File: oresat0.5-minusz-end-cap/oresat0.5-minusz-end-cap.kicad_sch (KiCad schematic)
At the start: 28 parts

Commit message: Updated both oresat0.5 end caps. Fixed layout, and added patch antennas
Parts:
- removed C1, C10, C2, C3, C7: (no value), symbol minusz-end-cap-eagle-import:C-EU0402-B-NOSILK
- removed C12, C13, C15, C19, C4: (no value), symbol minusz-end-cap-eagle-import:C-EU0603-B-NOSILK
- removed CF2: (no value), symbol minusz-end-cap-eagle-import:J-HARWIN-M55-70X1242R
- removed D2: (no value), symbol minusz-end-cap-eagle-import:LED-GREEN0603
- removed R1, R2, R3, R4, R5, R6, R7: (no value), symbol minusz-end-cap-eagle-import:R-US_0402-B-NOSILK
- removed TP1, TP2, TP3, TP4, TP6, TP7: (no value), symbol minusz-end-cap-eagle-import:TEST-POINT
- removed U1: (no value), symbol minusz-end-cap-eagle-import:TCA9543A-PW
- removed U3, U4: (no value), symbol minusz-end-cap-eagle-import:HMC5883L-LGA-16
- added ANT1: GP.1575.25.2.A.02, oresat-misc:Taoglas-GPS-Patch-Antenna, symbol Device:Antenna
- added C1, C10, C12, C13, C2, C3, C4, C7: (no value), oresat0.5-minusz-end-cap:.0603-B-NOSILK, symbol oresat0-plusz-end-cap-eagle-import:C-EU0603-B-NOSILK
- added D2: (no value), oresat0.5-minusz-end-cap:LED-0603, symbol oresat0-plusz-end-cap-eagle-import:LED-GREEN0603
- added J1: (no value), oresat0.5-minusz-end-cap:HARWIN-M55-70X1242R, symbol oresat0-plusz-end-cap-eagle-import:J-HARWIN-M55-70X1242R
- added J2: U.FL-R-SMA, Connector_Coaxial:U.FL_Hirose_U.FL-R-SMT-1_Vertical, symbol Connector:Conn_Coaxial
- added R1, R10, R2, R3, R4, R5, R6, R7, R8, R9: (no value), oresat0.5-minusz-end-cap:.0603-B-NOSILK, symbol oresat0-plusz-end-cap-eagle-import:R-US_0603-B-NOSILK
- added R11, R12: NP, oresat0.5-minusz-end-cap:.0603-B-NOSILK, symbol oresat0-plusz-end-cap-eagle-import:R-US_0603-B-NOSILK
- added TP1, TP2, TP3, TP4, TP5, TP6, TP7, TP8: TEST-POINT-LARGE-SQUARE, oresat0.5-minusz-end-cap:1X01, symbol oresat0-plusz-end-cap-eagle-import:TEST-POINT-LARGE-SQUARE
- added U1: (no value), oresat0.5-minusz-end-cap:16-SSOP, symbol oresat0-plusz-end-cap-eagle-import:LTC4305
- added U2, U3: (no value), oresat0.5-minusz-end-cap:LGA-16(3X3), symbol oresat0-plusz-end-cap-eagle-import:MMC5883MA
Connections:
- net 3.3V: now also C1.1, C10.1, C2.1, C3.1, C4.1, C7.1, J1.5, J1.6, R10.2, R2.2, R3.2, R4.2, R5.2, R6.2, R7.2, R8.2, TP7.1, U1.7 (VCC), U2.13 (VDDIO), U2.2 (VDD), U3.13 (VDDIO), U3.2 (VDD)
- net GND: now also C1.2, C10.2, C12.2, C13.2, C2.2, C3.2, C4.2, C7.2, D2.C, J1.7, J1.8, J1.P$1 (SHIELDS), J1.P$2 (SHIELDS), J1.P$3 (SHIELDS), J1.P$4 (SHIELDS), J2.2 (Ext), R1.1, R9.1, TP8.1, U1.10 (ADR2), U1.4 (GND), U1.8 (ADR0), U1.9 (ADR1), U2.11 (GND), U2.9 (GND), U3.11 (GND), U3.9 (GND)
- net I2C-SCL: now also J1.3, J1.4, TP3.1, U1.5 (SCLIN)
- net I2C-SDA: now also J1.1, J1.2, TP6.1, U1.3 (SDAIN)
- new net: C12.1, U3.10 (CAP)
- new net: ANT1.1 (A), J2.1 (In)
- new net: R11.1, U3.15 (INT)
- new net: R12.1, U2.15 (INT)
- new net: R12.2, R8.1, U1.1 (~{ALERT2})
- new net: R9.2, U1.11 (READY)
- new net: R11.2, R3.1, U1.14 (~{ALERT1})
- new net: R1.2, U1.2 (~{ALERT})
- new net: R10.1, U1.6 (ENABLE)
- new net: D2.A, R2.1
- new net: C13.1, U2.10 (CAP)
- new net SCL1: R7.1, TP1.1, U1.12 (SCL1), U3.1 (SCL)
- new net SCL2: R4.1, TP4.1, U1.16 (SCL2), U2.1 (SCL)
- new net SDA1: R6.1, TP2.1, U1.13 (SDA1), U3.16 (SDA)
- new net SDA2: R5.1, TP5.1, U1.15 (SDA2), U2.16 (SDA)
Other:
- note added: "+X-Y Corner"
- note added: "-X+Y Corner"
- note added: "1.0"
- note added: "OreSat0.5 -Z End Cap"
- note removed: "+X+Y Corner"
- note removed: "-X-Y Corner"
- note removed: "2.0"
- note removed: "All caps are 0402 ceramic 10% X5R Vw>=16V unless marked"
- note removed: "All resistors 0402 +/- 1% unless marked"
- note removed: "OreSat +Z End Card"

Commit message: Updated both OreSat0.5 end caps and cleaned up errors
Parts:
- C1, C10, C12, C13, C2, C3, C4, C7: symbol oresat0-plusz-end-cap-eagle-import:C-EU0603-B-NOSILK -> oresat0.5-minusz-end-cap-eagle-import:C-EU0603-B-NOSILK
- D2: symbol oresat0-plusz-end-cap-eagle-import:LED-GREEN0603 -> oresat0.5-minusz-end-cap-eagle-import:LED-GREEN0603
- J1: symbol oresat0-plusz-end-cap-eagle-import:J-HARWIN-M55-70X1242R -> oresat0.5-minusz-end-cap-eagle-import:J-HARWIN-M55-70X1242R
- R1, R10, R11, R12, R2, R3, R4, R5, R6, R7, R8, R9: symbol oresat0-plusz-end-cap-eagle-import:R-US_0603-B-NOSILK -> oresat0.5-minusz-end-cap-eagle-import:R-US_0603-B-NOSILK
- TP1, TP2, TP3, TP4, TP5, TP6, TP7, TP8: symbol oresat0-plusz-end-cap-eagle-import:TEST-POINT-LARGE-SQUARE -> oresat0.5-minusz-end-cap-eagle-import:TEST-POINT-LARGE-SQUARE
- U1: symbol oresat0-plusz-end-cap-eagle-import:LTC4305 -> oresat0.5-minusz-end-cap-eagle-import:LTC4305
- U2, U3: value (none) -> MMC5883MA; symbol oresat0-plusz-end-cap-eagle-import:MMC5883MA -> oresat0.5-minusz-end-cap-eagle-import:MMC5883MA
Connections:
- no-connect marks 0 -> 4
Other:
- moved on the sheet: ANT1, C1, C10, C12, C13, C2, C3, C4, C7, D2, J1, J2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

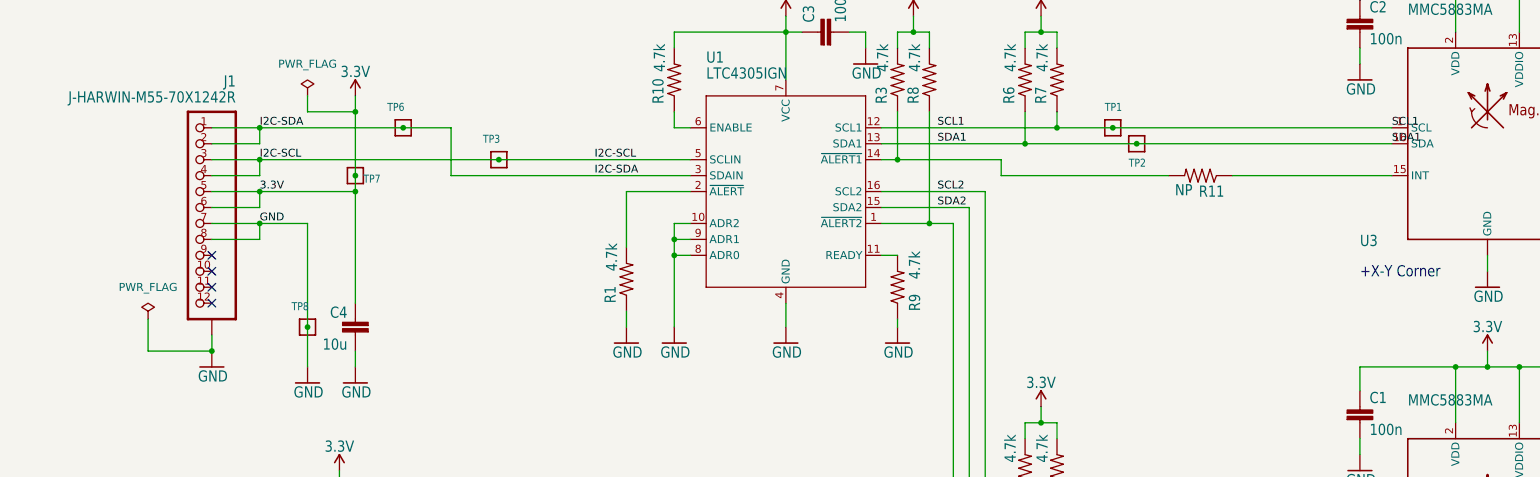
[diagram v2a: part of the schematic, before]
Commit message: OreSat0.5 end caps design review fixes
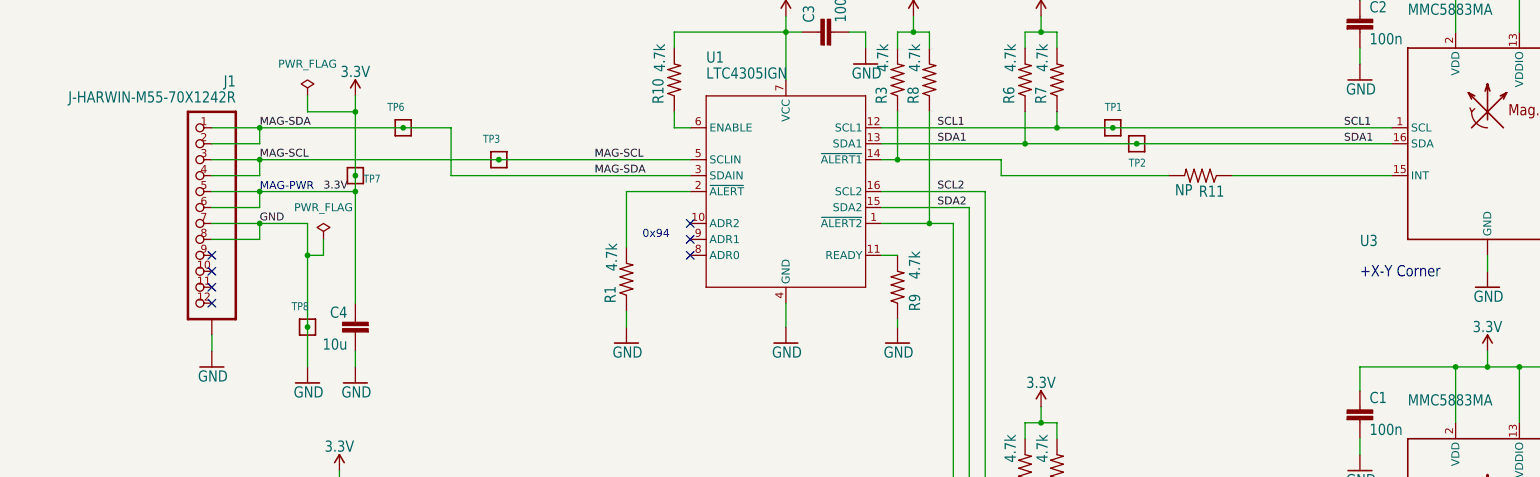
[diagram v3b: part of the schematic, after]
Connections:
- net GND: no longer U1.10 (ADR2), U1.8 (ADR0), U1.9 (ADR1)
- net I2C-SCL renamed MAG-SCL
- net I2C-SDA renamed MAG-SDA
- no-connect marks 4 -> 7
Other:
- note added: "0x94"
- note added: "MAG-PWR"
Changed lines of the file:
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@@
   (junction (at 124.46 119.38) (diameter 0) (color 0 0 0 0)
   )
-  (junction (at 175.26 132.08) (diameter 0) (color 0 0 0 0)
-  )
   (junction (at 193.04 96.52) (diameter 0) (color 0 0 0 0)
   )
@@
   (junction (at 233.68 158.75) (diameter 0) (color 0 0 0 0)
   )
-  (junction (at 175.26 129.54) (diameter 0) (color 0 0 0 0)
-  )
   (junction (at 304.8 88.9) (diameter 0) (color 0 0 0 0)
   )
+  (junction (at 116.84 132.08) (diameter 0) (color 0 0 0 0)
+  )
   (junction (at 233.68 96.52) (diameter 0) (color 0 0 0 0)
   )
@@
   )
   (junction (at 236.22 176.53) (diameter 0) (color 0 0 0 0)
-  )
-  (junction (at 101.6 147.32) (diameter 0) (color 0 0 0 0)
   )
   (no_connect (at 101.6 139.7))
@@
   (no_connect (at 101.6 137.16))
   (no_connect (at 101.6 134.62))
+  (no_connect (at 177.8 132.08))
+  (no_connect (at 177.8 129.54))
+  (no_connect (at 177.8 127))
   (wire (pts (xy 304.8 86.36) (xy 304.8 88.9))
     (stroke (width 0) (type default) (color 0 0 0 0))
@@
     (stroke (width 0) (type default) (color 0 0 0 0))
   )
-  (wire (pts (xy 91.44 147.32) (xy 91.44 142.24))
-    (stroke (width 0) (type default) (color 0 0 0 0))
-  )
   (wire (pts (xy 233.68 96.52) (xy 233.68 93.98))
     (stroke (width 0) (type default) (color 0 0 0 0))
@@
     (stroke (width 0) (type default) (color 0 0 0 0))
   )
-  (wire (pts (xy 175.26 129.54) (xy 177.8 129.54))
-    (stroke (width 0) (type default) (color 0 0 0 0))
-  )
   (wire (pts (xy 231.14 158.75) (xy 233.68 158.75))
     (stroke (width 0) (type default) (color 0 0 0 0))
@@
     (stroke (width 0) (type default) (color 0 0 0 0))
   )
+  (wire (pts (xy 116.84 132.08) (xy 119.38 132.08))
+    (stroke (width 0) (type default) (color 0 0 0 0))
+  )
   (wire (pts (xy 222.25 176.53) (xy 236.22 176.53))
     (stroke (width 0) (type default) (color 0 0 0 0))
@@
     (stroke (width 0) (type default) (color 0 0 0 0))
   )
-  (wire (pts (xy 175.26 143.51) (xy 175.26 132.08))
-    (stroke (width 0) (type default) (color 0 0 0 0))
-  )
   (wire (pts (xy 325.12 161.29) (xy 325.12 163.83))
     (stroke (width 0) (type default) (color 0 0 0 0))
@@
     (stroke (width 0) (type default) (color 0 0 0 0))
   )
-  (wire (pts (xy 175.26 132.08) (xy 175.26 129.54))
-    (stroke (width 0) (type default) (color 0 0 0 0))
-  )
   (wire (pts (xy 208.28 124.46) (xy 222.25 124.46))
     (stroke (width 0) (type default) (color 0 0 0 0))
@@
     (stroke (width 0) (type default) (color 0 0 0 0))
   )
-  (wire (pts (xy 175.26 127) (xy 177.8 127))
-    (stroke (width 0) (type default) (color 0 0 0 0))
-  )
   (wire (pts (xy 193.04 93.98) (xy 193.04 96.52))
     (stroke (width 0) (type default) (color 0 0 0 0))
@@
     (stroke (width 0) (type default) (color 0 0 0 0))
   )
-  (wire (pts (xy 175.26 132.08) (xy 177.8 132.08))
-    (stroke (width 0) (type default) (color 0 0 0 0))
-  )
   (wire (pts (xy 299.72 88.9) (xy 304.8 88.9))
     (stroke (width 0) (type default) (color 0 0 0 0))
   )
-  (wire (pts (xy 175.26 129.54) (xy 175.26 127))
-    (stroke (width 0) (type default) (color 0 0 0 0))
-  )
   (wire (pts (xy 236.22 171.45) (xy 236.22 176.53))
     (stroke (width 0) (type default) (color 0 0 0 0))
@@
     (stroke (width 0) (type default) (color 0 0 0 0))
   )
-  (wire (pts (xy 101.6 147.32) (xy 91.44 147.32))
+  (wire (pts (xy 116.84 132.08) (xy 116.84 143.51))
     (stroke (width 0) (type default) (color 0 0 0 0))
   )
@@
     (stroke (width 0) (type default) (color 0 0 0 0))
   )
-  (wire (pts (xy 116.84 127) (xy 116.84 143.51))
+  (wire (pts (xy 116.84 127) (xy 116.84 132.08))
     (stroke (width 0) (type default) (color 0 0 0 0))
   )
@@
   )
   (wire (pts (xy 248.92 114.3) (xy 231.14 114.3))
+    (stroke (width 0) (type default) (color 0 0 0 0))
+  )
+  (wire (pts (xy 119.38 129.54) (xy 119.38 132.08))
     (stroke (width 0) (type default) (color 0 0 0 0))
   )
@@
     (effects (font (size 2.032 2.032)) (justify left bottom))
   )
-  (label "I2C-SCL" (at 109.22 116.84 0)
+  (text "MAG-PWR" (at 109.22 121.92 0)
+    (effects (font (size 1.27 1.27)) (justify left bottom))
+  )
+  (text "0x94" (at 170.18 129.54 0)
+    (effects (font (size 1.27 1.27)) (justify left bottom))
+  )
+  (label "MAG-SCL" (at 109.22 116.84 0)
     (effects (font (size 1.2446 1.2446)) (justify left bottom))
   )
-  (label "I2C-SDA" (at 109.22 111.76 0)
+  (label "MAG-SDA" (at 109.22 111.76 0)
     (effects (font (size 1.2446 1.2446)) (justify left bottom))
   )
@@
     (effects (font (size 1.2446 1.2446)) (justify left bottom))
   )
-  (label "SCL1" (at 289.56 111.76 0)
+  (label "SCL1" (at 281.94 111.76 0)
     (effects (font (size 1.2446 1.2446)) (justify left bottom))
   )
-  (label "I2C-SDA" (at 162.56 119.38 0)
+  (label "MAG-SDA" (at 162.56 119.38 0)
     (effects (font (size 1.2446 1.2446)) (justify left bottom))
   )
-  (label "3.3V" (at 109.22 121.92 0)
+  (label "3.3V" (at 119.38 121.92 0)
     (effects (font (size 1.2446 1.2446)) (justify left bottom))
   )
@@
     (effects (font (size 1.2446 1.2446)) (justify left bottom))
   )
-  (label "I2C-SCL" (at 162.56 116.84 0)
+  (label "MAG-SCL" (at 162.56 116.84 0)
     (effects (font (size 1.2446 1.2446)) (justify left bottom))
   )
-  (label "SDA1" (at 289.56 114.3 0)
+  (label "SDA1" (at 281.94 114.3 0)
     (effects (font (size 1.2446 1.2446)) (justify left bottom))
   )
@@
     (pin "1")
   )
-  (symbol (lib_id "oresat0.5-minusz-end-cap-eagle-import:GND") (at 175.26 146.05 0) (mirror y) (unit 1)
-    (in_bom yes) (on_board yes)
-    (property "Reference" "#GND0103" (id 0) (at 175.26 146.05 0)
-      (effects (font (size 1.27 1.27)) hide)
-    )
-    (property "Value" "GND" (id 1) (at 177.8 148.59 0)
-      (effects (font (size 1.778 1.5113)) (justify left bottom))
-    )
-    (property "Footprint" "oresat0-plusz-end-cap:" (id 2) (at 175.26 146.05 0)
-      (effects (font (size 1.27 1.27)) hide)
-    )
-    (property "Datasheet" "" (id 3) (at 175.26 146.05 0)
-      (effects (font (size 1.27 1.27)) hide)
-    )
-    (pin "1")
-  )
   (symbol (lib_id "oresat0.5-minusz-end-cap-eagle-import:GND") (at 116.84 152.4 0) (mirror y) (unit 1)
     (in_bom yes) (on_board yes)
@@
     (pin "2")
   )
-  (symbol (lib_id "power:PWR_FLAG") (at 91.44 142.24 0) (unit 1)
+  (symbol (lib_id "power:PWR_FLAG") (at 119.38 129.54 0) (unit 1)
     (in_bom yes) (on_board yes) (fields_autoplaced)
-    (property "Reference" "#FLG0101" (id 0) (at 91.44 140.335 0)
-      (effects (font (size 1.27 1.27)) hide)
-    )
-    (property "Value" "PWR_FLAG" (id 1) (at 91.44 137.16 0))
-    (property "Footprint" "" (id 2) (at 91.44 142.24 0)
-      (effects (font (size 1.27 1.27)) hide)
-    )
-    (property "Datasheet" "~" (id 3) (at 91.44 142.24 0)
+    (property "Reference" "#FLG0101" (id 0) (at 119.38 127.635 0)
+      (effects (font (size 1.27 1.27)) hide)
+    )
+    (property "Value" "PWR_FLAG" (id 1) (at 119.38 124.46 0))
+    (property "Footprint" "" (id 2) (at 119.38 129.54 0)
+      (effects (font (size 1.27 1.27)) hide)
+    )
+    (property "Datasheet" "~" (id 3) (at 119.38 129.54 0)
       (effects (font (size 1.27 1.27)) hide)
     )
@@
       (reference "#GND0102") (unit 1) (value "GND") (footprint "oresat0-plusz-end-cap:")
     )
-    (path "/3d14e0e7-82bc-4dbb-9e62-5a07bc58df6c"
-      (reference "#GND0103") (unit 1) (value "GND") (footprint "oresat0-plusz-end-cap:")
-    )
     (path "/a60a1df8-eb53-419a-845c-a317b6139ba4"

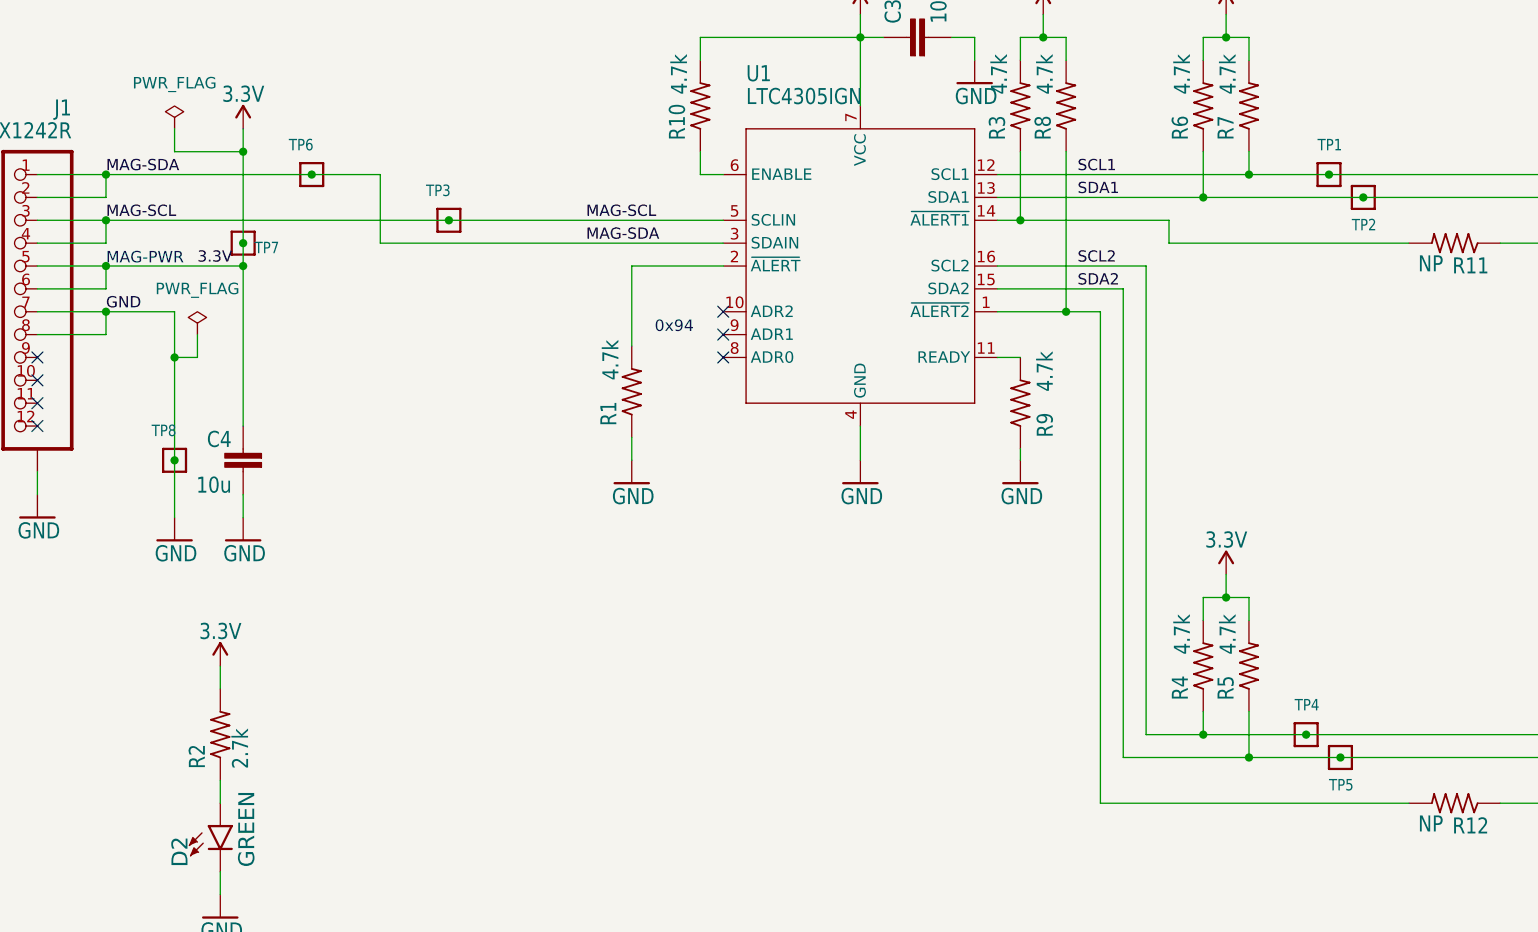
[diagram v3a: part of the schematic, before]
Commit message: Updated end caps
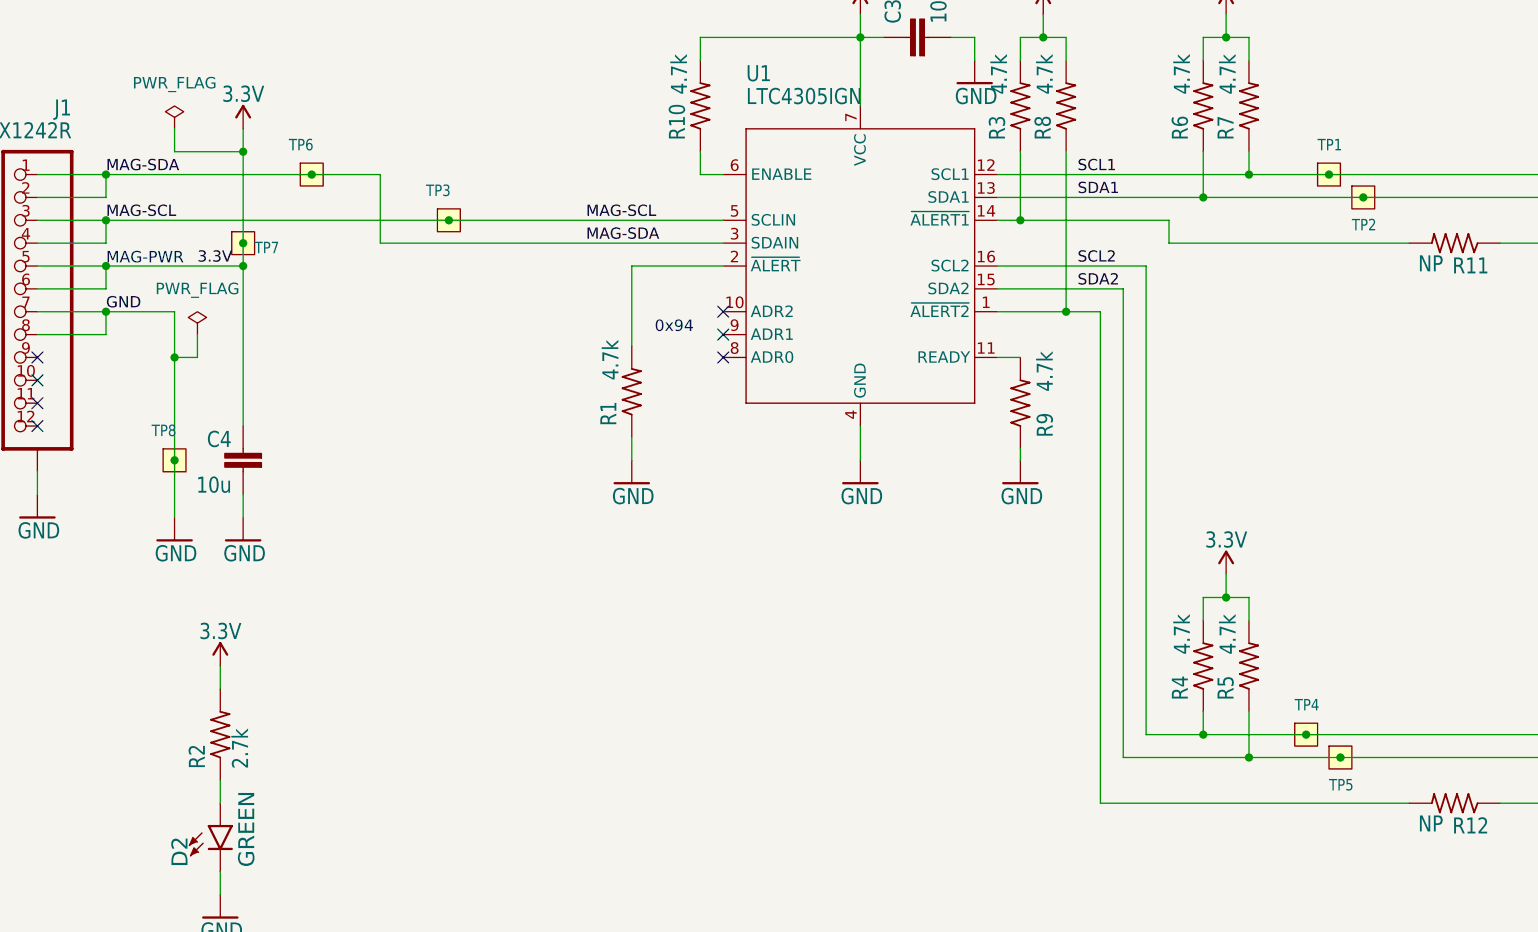
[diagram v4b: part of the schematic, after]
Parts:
- TP1, TP2, TP3, TP4, TP5, TP6, TP7, TP8: footprint oresat0.5-minusz-end-cap:1X01 -> oresat-misc:TestPoint-0.75mm-th; symbol oresat0.5-minusz-end-cap-eagle-import:TEST-POINT-LARGE-SQUARE -> oresat-misc:Test-Point-0.75mm-th

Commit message: Updated mounting holes
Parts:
- U2, U3: footprint oresat0.5-minusz-end-cap:LGA-16(3X3) -> oresat0-plusz-end-cap:LGA-16(3X3)
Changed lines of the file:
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@@
       (effects (font (size 1.778 1.5113)) (justify left bottom))
     )
-    (property "Footprint" "oresat0.5-minusz-end-cap:LGA-16(3X3)" (at 304.8 114.3 0)
+    (property "Footprint" "oresat0-plusz-end-cap:LGA-16(3X3)" (at 304.8 114.3 0)
       (effects (font (size 1.27 1.27)) hide)
     )
@@
     (pin "2")
     (pin "9")
+    (pin "12")
+    (pin "14")
+    (pin "3")
+    (pin "4")
+    (pin "5")
+    (pin "6")
+    (pin "7")
+    (pin "8")
     (instances
       (project "oresat0.5-minusz-end-cap"
@@
       (effects (font (size 1.778 1.5113)) (justify left bottom))
     )
-    (property "Footprint" "oresat0.5-minusz-end-cap:LGA-16(3X3)" (at 304.8 176.53 0)
+    (property "Footprint" "oresat0-plusz-end-cap:LGA-16(3X3)" (at 304.8 176.53 0)
       (effects (font (size 1.27 1.27)) hide)
     )
@@
     (pin "2")
     (pin "9")
-    (instances
-      (project "oresat0.5-minusz-end-cap"
+    (pin "12")
+    (pin "14")
+    (pin "3")
+    (pin "4")
+    (pin "5")
+    (pin "6")
+    (pin "7")
+    (pin "8")
+    (instances
+      (project "oresat0.5-minusz-end-cap"
